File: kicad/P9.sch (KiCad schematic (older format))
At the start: 10 parts, among them J1 addr, P4 CONN_23X2, U1 BEAGLEBONE, U2 CAT24C256

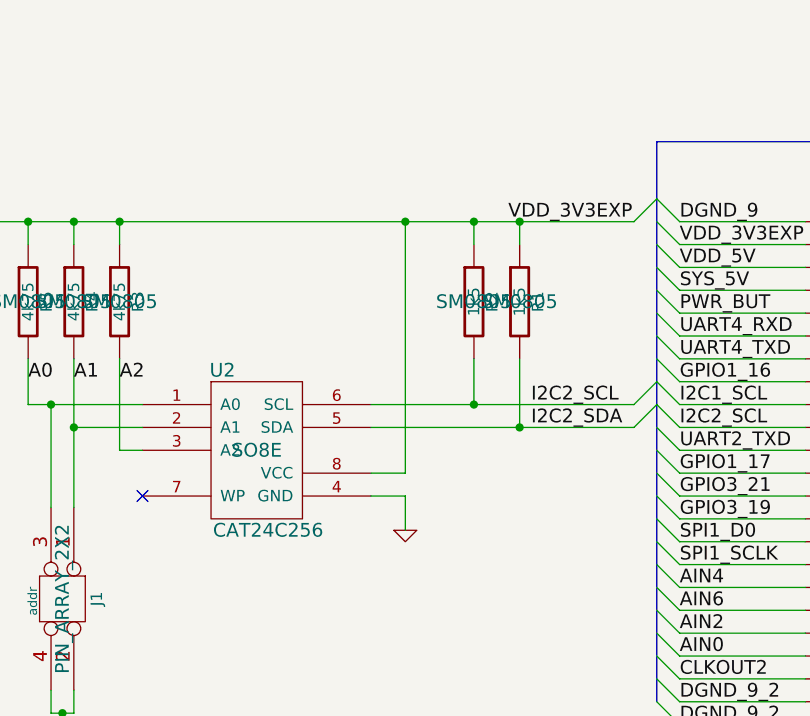
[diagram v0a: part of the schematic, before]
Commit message: with fastrax gps, lsm303 footprint, ad7193
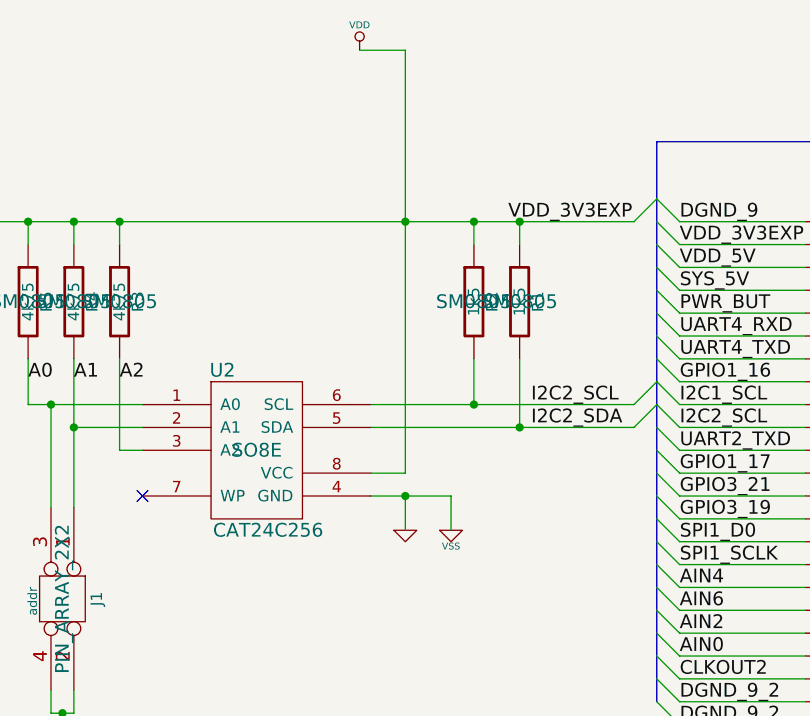
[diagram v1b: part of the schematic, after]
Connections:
- net VDD_3V3EXP renamed VDD
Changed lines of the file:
@@
-EESchema Schematic File Version 2  date Wed 09 Oct 2013 04:26:28 PM EDT
+EESchema Schematic File Version 2  date Thu 24 Oct 2013 03:20:39 PM EDT
 LIBS:power
 LIBS:device
@@
 LIBS:FlyingBone-cache
 LIBS:beaglebone
+LIBS:p8x32a-lqfp
+LIBS:IHE
+LIBS:dallas-rtc
+LIBS:freescale-accelerometer
+LIBS:SparkFun
 LIBS:FlyingBone-cache
 EELAYER 25  0
@@
 Sheet 3 5
 Title "FlyingBone - Proto board for BeagleBone"
-Date "9 oct 2013"
+Date "24 oct 2013"
 Rev "0.3"
 Comp "Jacek Radzikowski <jacek.radzikowski@gmail.com>"
@@
 Comment4 ""
 $EndDescr
+Connection ~ 3650 3750
+Wire Wire Line
+	3500 3750 3850 3750
+Wire Wire Line
+	3850 3750 3850 3900
 Wire Wire Line
 	4650 2550 1700 2550
 Wire Wire Line
-	3650 3900 3650 3750
-Wire Wire Line
-	3650 3750 3500 3750
+	3650 3750 3650 3900
 Wire Wire Line
 	3500 3450 4650 3450
@@
 Wire Wire Line
 	3500 3650 3650 3650
-Wire Wire Line
-	3650 3650 3650 2550
 Connection ~ 3650 2550
 Wire Wire Line
 	3950 2650 3950 2550
 Connection ~ 3950 2550
+Wire Wire Line
+	3650 3650 3650 1800
+Wire Wire Line
+	3650 1800 3450 1800
+$Comp
+L VSS #PWR15
+U 1 1 525F0099
+P 3850 3900
+F 0 "#PWR15" H 3850 3900 30  0001 C CNN
+F 1 "VSS" H 3850 3830 30  0000 C CNN
+	1    3850 3900
+	1    0    0    -1
+$EndComp
+$Comp
+L VDD #PWR13
+U 1 1 525F0073
+P 3450 1800
+F 0 "#PWR13" H 3450 1900 30  0001 C CNN
+F 1 "VDD" H 3450 1910 30  0000 C CNN
+	1    3450 1800
+	1    0    0    -1
+$EndComp
 Text Label 2000 3250 0    60   ~ 0
 A0
@@
 A2
 $Comp
-L GND #PWR01
+L GND #PWR14
 U 1 1 4EB9CD38
 P 3650 3900
-F 0 "#PWR01" H 3650 3900 30  0001 C CNN
+F 0 "#PWR14" H 3650 3900 30  0001 C CNN
 F 1 "GND" H 3650 3830 30  0001 C CNN
 	1    3650 3900
@@
 $EndComp
 $Comp
-L GND #PWR02
+L GND #PWR11
 U 1 1 4EB9CBD3
 P 1700 3300
-F 0 "#PWR02" H 1700 3300 30  0001 C CNN
+F 0 "#PWR11" H 1700 3300 30  0001 C CNN
 F 1 "GND" H 1700 3230 30  0001 C CNN
 	1    1700 3300
@@
 $EndComp
 $Comp
-L GND #PWR03
+L GND #PWR12
 U 1 1 4EB9CB8D
 P 2150 4800
-F 0 "#PWR03" H 2150 4800 30  0001 C CNN
+F 0 "#PWR12" H 2150 4800 30  0001 C CNN
 F 1 "GND" H 2150 4730 30  0001 C CNN
 	1    2150 4800
@@
 $EndComp
 $Comp
-L GND #PWR04
+L GND #PWR16
 U 1 1 4EB48FA3
 P 9600 2200
-F 0 "#PWR04" H 9600 2200 30  0001 C CNN
+F 0 "#PWR16" H 9600 2200 30  0001 C CNN
 F 1 "GND" H 9600 2130 30  0001 C CNN
 	1    9600 2200
